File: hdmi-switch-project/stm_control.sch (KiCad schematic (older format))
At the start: 36 parts, among them U2 TCAN330, U3 STM32F103C8Tx

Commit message: Cosmetical changes, and VSDJ pin fixup
Signed-off-by: Andrej Manduch <amanduch@gmail.com>
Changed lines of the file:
@@
 encoding utf-8
 Sheet 4 4
-Title ""
-Date ""
+Title "HDMI Switch 4:2 modul"
+Date "2020-06-30"
 Rev ""
 Comp ""
-Comment1 ""
+Comment1 "Devel board"
 Comment2 ""
 Comment3 ""
@@
 $EndComp
 Entry Wire Line
-	4950 2450 5050 2550
-Entry Wire Line
-	4950 2550 5050 2650
-Entry Wire Line
-	4950 2750 5050 2850
-Entry Wire Line
-	4950 2850 5050 2950
-Entry Wire Line
-	4950 2950 5050 3050
-Entry Wire Line
-	4950 3950 5050 4050
-Entry Wire Line
-	4950 4050 5050 4150
-Entry Wire Line
-	4950 4150 5050 4250
-Entry Wire Line
-	4950 4250 5050 4350
-Wire Wire Line
-	5800 4350 5050 4350
-Wire Wire Line
-	5050 4250 5800 4250
-Wire Wire Line
-	5050 3050 5800 3050
-Wire Wire Line
-	5800 2950 5050 2950
-Wire Wire Line
-	5050 2850 5800 2850
-Wire Wire Line
-	5800 2650 5050 2650
-Wire Wire Line
-	5050 2550 5800 2550
+	5050 2450 5150 2550
+Entry Wire Line
+	5050 2550 5150 2650
+Entry Wire Line
+	5050 2750 5150 2850
+Entry Wire Line
+	5050 2850 5150 2950
+Entry Wire Line
+	5050 2950 5150 3050
+Entry Wire Line
+	5050 3950 5150 4050
+Entry Wire Line
+	5050 4050 5150 4150
+Entry Wire Line
+	5050 4150 5150 4250
+Entry Wire Line
+	5050 4250 5150 4350
+Wire Wire Line
+	5800 4350 5150 4350
+Wire Wire Line
+	5150 4250 5800 4250
+Wire Wire Line
+	5150 3050 5800 3050
+Wire Wire Line
+	5800 2950 5150 2950
+Wire Wire Line
+	5150 2850 5800 2850
+Wire Wire Line
+	5800 2650 5150 2650
+Wire Wire Line
+	5150 2550 5800 2550
 $Comp
 L Device:C C_XTAL11
@@
 Wire Wire Line
 	8850 2350 8950 2350
-Text Label 5050 2950 0    50   ~ 0
+Text Label 5150 2950 0    50   ~ 0
 XTAL2_RTC_A
-Text Label 5050 3050 0    50   ~ 0
+Text Label 5150 3050 0    50   ~ 0
 XTAL2_RTC_B
 Entry Wire Line
@@
 Text Label 10250 2800 0    50   ~ 0
 XTAL2_RTC_B
-Text Label 5050 2550 0    50   ~ 0
+Text Label 5150 2550 0    50   ~ 0
 XTAL1_A
-Text Label 5050 2650 0    50   ~ 0
+Text Label 5150 2650 0    50   ~ 0
 XTAL1_B
 $Comp
@@
 	1050 3150 1050 3100
 Entry Wire Line
-	7850 4650 7950 4750
-Entry Wire Line
-	7850 4550 7950 4650
-Entry Wire Line
-	7850 4450 7950 4550
-Entry Wire Line
-	7850 4350 7950 4450
-Wire Wire Line
-	7850 4350 7100 4350
-Wire Wire Line
-	7100 4450 7850 4450
+	7650 4650 7750 4750
+Entry Wire Line
+	7650 4550 7750 4650
+Entry Wire Line
+	7650 4450 7750 4550
+Entry Wire Line
+	7650 4350 7750 4450
+Wire Wire Line
+	7650 4350 7100 4350
+Wire Wire Line
+	7100 4450 7650 4450
 Text Label 7150 4350 0    50   ~ 0
 USB1_D-
@@
 $EndComp
 Wire Wire Line
-	7100 4650 7850 4650
+	7100 4650 7650 4650
 Text Label 7150 4650 0    50   ~ 0
 STM_SWDCLCK
 Wire Wire Line
-	7100 4550 7850 4550
+	7100 4550 7650 4550
 Text Label 7150 4550 0    50   ~ 0
 STM_SWDIO
@@
 Wire Notes Line
 	550  3300 550  5250
-Text Label 5050 3450 0    50   ~ 0
+Text Label 5150 3450 0    50   ~ 0
 STM_BOOT1
 Entry Wire Line
-	4950 2250 5050 2350
-Wire Wire Line
-	5800 2350 5050 2350
-Text Label 5050 2350 0    50   ~ 0
+	5050 2250 5150 2350
+Wire Wire Line
+	5800 2350 5150 2350
+Text Label 5150 2350 0    50   ~ 0
 STM_BOOT0
 $Comp
@@
 Wire Wire Line
 	2000 4950 2100 4950
-Text HLabel 5500 3850 0    50   Input ~ 0
+Text HLabel 5600 3850 0    50   Input ~ 0
 ST_H_CLK
-Text HLabel 5500 3950 0    50   Input ~ 0
+Text HLabel 5600 3950 0    50   Input ~ 0
 ST_H_SDA
 Wire Wire Line
-	5500 3850 5800 3850
-Wire Wire Line
-	5800 3950 5500 3950
-Wire Wire Line
-	5050 4050 5800 4050
-Wire Wire Line
-	5800 4150 5050 4150
-Text Label 5050 4050 0    50   ~ 0
+	5600 3850 5800 3850
+Wire Wire Line
+	5800 3950 5600 3950
+Wire Wire Line
+	5150 4050 5800 4050
+Wire Wire Line
+	5800 4150 5150 4150
+Text Label 5150 4050 0    50   ~ 0
 STM_CAN_RX
-Text Label 5050 4150 0    50   ~ 0
+Text Label 5150 4150 0    50   ~ 0
 STM_CAN_TX
-Text Label 5050 4350 0    50   ~ 0
+Text Label 5150 4350 0    50   ~ 0
 STM_CNTRL_SDA
-Text Label 5050 4250 0    50   ~ 0
+Text Label 5150 4250 0    50   ~ 0
 STM_CNTRL_CLK
 Text Label 7150 4250 0    50   ~ 0
@@
 STM_TX
 Entry Wire Line
-	7850 4250 7950 4350
-Entry Wire Line
-	7850 4150 7950 4250
-Wire Wire Line
-	7100 4150 7850 4150
-Wire Wire Line
-	7100 4250 7850 4250
+	7650 4250 7750 4350
+Entry Wire Line
+	7650 4150 7750 4250
+Wire Wire Line
+	7100 4150 7650 4150
+Wire Wire Line
+	7100 4250 7650 4250
 Text HLabel 7200 3250 2    50   Input ~ 0
 STM_GPIO0
@@
 STM_GPIO7
 Wire Wire Line
-	5050 3450 5800 3450
-Entry Wire Line
-	4950 3350 5050 3450
+	5150 3450 5800 3450
+Entry Wire Line
+	5050 3350 5150 3450
 Wire Wire Line
 	7200 3950 7100 3950
@@
 Wire Wire Line
 	7100 3250 7200 3250
-Text HLabel 5700 3350 0    50   Input ~ 0
+Text HLabel 5600 3350 0    50   Input ~ 0
 STM_GPIO
-Text HLabel 5700 3250 0    50   Input ~ 0
+Text HLabel 5600 3250 0    50   Input ~ 0
 STM_GE
-Text HLabel 5700 3550 0    50   Input ~ 0
+Text HLabel 5600 3550 0    50   Input ~ 0
 STM_A0
-Text HLabel 5700 3650 0    50   Input ~ 0
+Text HLabel 5600 3650 0    50   Input ~ 0
 STM_A1
 Wire Wire Line
-	5700 3250 5800 3250
-Wire Wire Line
-	5800 3350 5700 3350
-Wire Wire Line
-	5700 3550 5800 3550
-Wire Wire Line
-	5800 3650 5700 3650
+	5600 3250 5800 3250
+Wire Wire Line
+	5800 3350 5600 3350
+Wire Wire Line
+	5600 3550 5800 3550
+Wire Wire Line
+	5800 3650 5600 3650
 Text HLabel 7200 4050 2    50   Input ~ 0
 STM_GPIO8
@@
 Wire Wire Line
 	3200 1300 3200 1200
-Text Label 5050 2850 0    50   ~ 0
+Text Label 5150 2850 0    50   ~ 0
 STM_LED1
 $Comp
@@
 	5650 2150 5800 2150
 Entry Wire Line
-	4950 4650 5050 4750
-Wire Wire Line
-	5800 4750 5050 4750
-Text Label 5050 4750 0    50   ~ 0
+	5050 4650 5150 4750
+Wire Wire Line
+	5800 4750 5150 4750
+Text Label 5150 4750 0    50   ~ 0
 STM_BTN1
 Wire Notes Line
@@
 Wire Notes Line
 	4600 700  4600 3000
-Text HLabel 5700 3750 0    50   Input ~ 0
+Text HLabel 5600 3750 0    50   Input ~ 0
 STM_OVS
 Wire Wire Line
-	5800 3750 5700 3750
+	5800 3750 5600 3750
 Wire Bus Line
 	4200 2050 4200 2450
@@
 	10850 1450 10850 2950
 Wire Bus Line
-	7950 1900 7950 4850
+	7750 4150 7750 4850
 Wire Bus Line
-	4950 1850 4950 4850
+	5050 2200 5050 4850
 $EndSCHEMATC

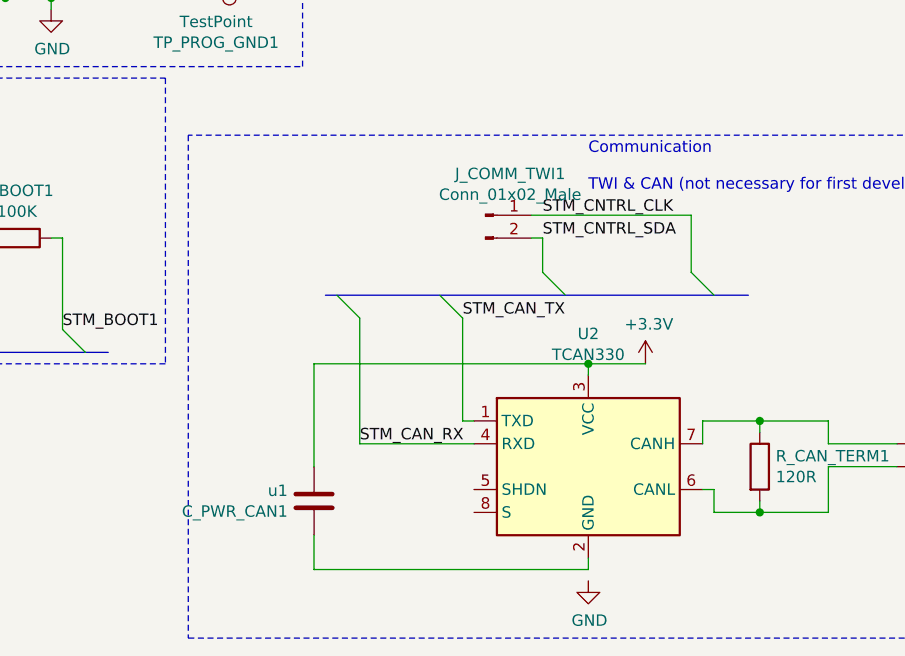
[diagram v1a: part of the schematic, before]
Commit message: Precission resistor changed
from 4k6 to 4k64 %1

Signed-off-by: Andrej Manduch <amanduch@gmail.com>
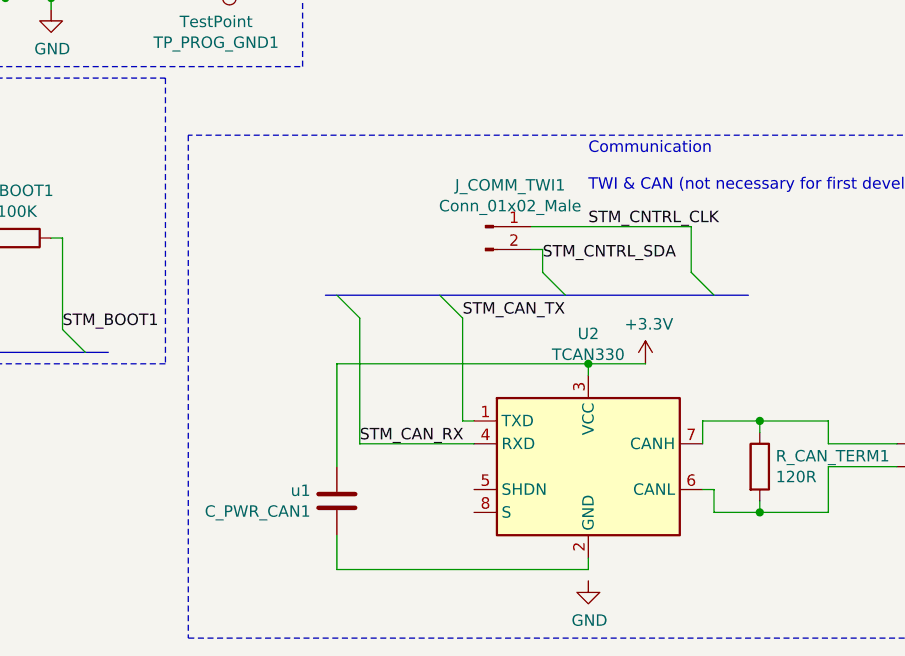
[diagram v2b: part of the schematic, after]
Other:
- moved on the sheet: C_PWR_CAN1, J_COMM_TWI1
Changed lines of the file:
@@
 	3650 6350 3650 6900
 Wire Wire Line
-	3450 6550 3450 7000
+	3550 6550 3550 7000
 Connection ~ 4650 6550
 Wire Wire Line
@@
 	4650 7450 4650 7400
 Wire Wire Line
-	3450 7450 4650 7450
-Wire Wire Line
-	3450 7300 3450 7450
-Wire Wire Line
-	4650 6550 3450 6550
+	3550 7450 4650 7450
+Wire Wire Line
+	3550 7300 3550 7450
+Wire Wire Line
+	4650 6550 3550 6550
 Wire Wire Line
 	4650 6600 4650 6550
-$Comp
-L Device:C C_PWR_CAN1
-U 1 1 5FF842AA
-P 3450 7150
-F 0 "C_PWR_CAN1" H 3565 7196 50  0000 L CNN
-F 1 "u1" H 3565 7105 50  0000 L CNN
-F 2 "" H 3488 7000 50  0001 C CNN
-F 3 "~" H 3450 7150 50  0001 C CNN
-	1    3450 7150
-	-1   0    0    1
-$EndComp
 Wire Wire Line
 	3650 6900 4150 6900
@@
 $EndComp
 Wire Wire Line
-	4400 5900 5100 5900
-Text Label 4450 5900 0    50   ~ 0
+	4400 5950 5100 5950
+Text Label 4650 5950 0    50   ~ 0
 STM_CNTRL_CLK
-Text Label 4450 6000 0    50   ~ 0
+Text Label 4450 6100 0    50   ~ 0
 STM_CNTRL_SDA
 Wire Wire Line
-	5100 6150 5100 5900
-Wire Wire Line
-	4450 6000 4400 6000
+	5100 6150 5100 5950
+Wire Wire Line
+	4450 6050 4400 6050
 Entry Wire Line
 	5100 6150 5200 6250
@@
 	4450 6150 4550 6250
 Wire Wire Line
-	4450 6150 4450 6000
+	4450 6150 4450 6050
 $Comp
 L Connector:Conn_01x02_Male J_COMM_TWI1
 U 1 1 5FE65265
-P 4200 5900
-F 0 "J_COMM_TWI1" H 4308 6081 50  0000 C CNN
-F 1 "Conn_01x02_Male" H 4308 5990 50  0000 C CNN
-F 2 "" H 4200 5900 50  0001 C CNN
-F 3 "~" H 4200 5900 50  0001 C CNN
-	1    4200 5900
+P 4200 5950
+F 0 "J_COMM_TWI1" H 4308 6131 50  0000 C CNN
+F 1 "Conn_01x02_Male" H 4308 6040 50  0000 C CNN
+F 2 "" H 4200 5950 50  0001 C CNN
+F 3 "~" H 4200 5950 50  0001 C CNN
+	1    4200 5950
 	1    0    0    -1
 $EndComp
@@
 Wire Wire Line
 	5800 3750 5600 3750
+$Comp
+L Device:C C_PWR_CAN1
+U 1 1 5FF842AA
+P 3550 7150
+F 0 "C_PWR_CAN1" H 3665 7196 50  0000 L CNN
+F 1 "u1" H 3665 7105 50  0000 L CNN
+F 2 "" H 3588 7000 50  0001 C CNN
+F 3 "~" H 3550 7150 50  0001 C CNN
+	1    3550 7150
+	-1   0    0    1
+$EndComp
 Wire Bus Line
 	4200 2050 4200 2450

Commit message: placed UART connector
Signed-off-by: Andrej Manduch <amanduch@gmail.com>
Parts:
- added J_UART: Conn_01x03_Male, symbol Connector:Conn_01x03_Male
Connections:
- net GND: now also J_UART.3 (Pin_3)
- net STM_RX: now also J_UART.2 (Pin_2)
- net STM_TX: now also J_UART.1 (Pin_1)
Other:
- note added: "Service UART"
- moved on the sheet: C_BUTTON1, D_LED1, R_BTN1, R_LED1, SW_STM1
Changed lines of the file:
@@
 L power:+3.3V #PWR020
 U 1 1 6001D411
-P 3200 1200
-F 0 "#PWR020" H 3200 1050 50  0001 C CNN
-F 1 "+3.3V" H 3215 1373 50  0000 C CNN
-F 2 "" H 3200 1200 50  0001 C CNN
-F 3 "" H 3200 1200 50  0001 C CNN
-	1    3200 1200
-	1    0    0    -1
-$EndComp
-Wire Wire Line
-	3200 1300 3200 1200
+P 3050 1050
+F 0 "#PWR020" H 3050 900 50  0001 C CNN
+F 1 "+3.3V" H 3065 1223 50  0000 C CNN
+F 2 "" H 3050 1050 50  0001 C CNN
+F 3 "" H 3050 1050 50  0001 C CNN
+	1    3050 1050
+	1    0    0    -1
+$EndComp
+Wire Wire Line
+	3050 1150 3050 1050
 Text Label 5150 2850 0    50   ~ 0
 STM_LED1
@@
 STM_BTN1
 Wire Notes Line
-	4400 1550 4400 3000
-Text Notes 3750 1800 0    50   ~ 0
+	4250 1400 4250 2850
+Text Notes 3600 1650 0    50   ~ 0
 Example Button
 Entry Wire Line
-	4100 2200 4200 2300
-Wire Wire Line
-	3600 2200 4100 2200
-Text Label 3700 2200 0    50   ~ 0
+	3950 2050 4050 2150
+Wire Wire Line
+	3450 2050 3950 2050
+Text Label 3550 2050 0    50   ~ 0
 STM_BTN1
-Connection ~ 3600 2700
-Wire Wire Line
-	3600 2750 3600 2700
-Wire Wire Line
-	3600 1850 3600 1800
-Connection ~ 3600 2200
-Wire Wire Line
-	3600 2200 3600 2150
+Connection ~ 3450 2550
+Wire Wire Line
+	3450 2600 3450 2550
+Wire Wire Line
+	3450 1700 3450 1650
+Connection ~ 3450 2050
+Wire Wire Line
+	3450 2050 3450 2000
 $Comp
 L power:+3.3V #PWR021
 U 1 1 600B8EEF
-P 3600 1800
-F 0 "#PWR021" H 3600 1650 50  0001 C CNN
-F 1 "+3.3V" H 3615 1973 50  0000 C CNN
-F 2 "" H 3600 1800 50  0001 C CNN
-F 3 "" H 3600 1800 50  0001 C CNN
-	1    3600 1800
+P 3450 1650
+F 0 "#PWR021" H 3450 1500 50  0001 C CNN
+F 1 "+3.3V" H 3465 1823 50  0000 C CNN
+F 2 "" H 3450 1650 50  0001 C CNN
+F 3 "" H 3450 1650 50  0001 C CNN
+	1    3450 1650
 	1    0    0    -1
 $EndComp
@@
 L Device:R R_BTN1
 U 1 1 600B8B61
-P 3600 2000
-F 0 "R_BTN1" H 3670 2046 50  0000 L CNN
-F 1 "10K" H 3670 1955 50  0000 L CNN
-F 2 "" V 3530 2000 50  0001 C CNN
-F 3 "~" H 3600 2000 50  0001 C CNN
-	1    3600 2000
+P 3450 1850
+F 0 "R_BTN1" H 3520 1896 50  0000 L CNN
+F 1 "10K" H 3520 1805 50  0000 L CNN
+F 2 "" V 3380 1850 50  0001 C CNN
+F 3 "~" H 3450 1850 50  0001 C CNN
+	1    3450 1850
 	1    0    0    -1
 $EndComp
@@
 L power:GND #PWR022
 U 1 1 600B8434
-P 3600 2750
-F 0 "#PWR022" H 3600 2500 50  0001 C CNN
-F 1 "GND" H 3605 2577 50  0000 C CNN
-F 2 "" H 3600 2750 50  0001 C CNN
-F 3 "" H 3600 2750 50  0001 C CNN
-	1    3600 2750
-	1    0    0    -1
-$EndComp
-Wire Wire Line
-	3600 2700 3600 2600
-Wire Wire Line
-	3450 2700 3600 2700
-Wire Wire Line
-	3450 2650 3450 2700
-Wire Wire Line
-	3600 2200 3600 2300
-Wire Wire Line
-	3450 2200 3600 2200
-Wire Wire Line
-	3450 2250 3450 2200
+P 3450 2600
+F 0 "#PWR022" H 3450 2350 50  0001 C CNN
+F 1 "GND" H 3455 2427 50  0000 C CNN
+F 2 "" H 3450 2600 50  0001 C CNN
+F 3 "" H 3450 2600 50  0001 C CNN
+	1    3450 2600
+	1    0    0    -1
+$EndComp
+Wire Wire Line
+	3450 2550 3450 2450
+Wire Wire Line
+	3300 2550 3450 2550
+Wire Wire Line
+	3300 2500 3300 2550
+Wire Wire Line
+	3450 2050 3450 2150
+Wire Wire Line
+	3300 2050 3450 2050
+Wire Wire Line
+	3300 2100 3300 2050
 $Comp
 L Device:C C_BUTTON1
 U 1 1 60092EA5
-P 3600 2450
-F 0 "C_BUTTON1" H 3715 2496 50  0000 L CNN
-F 1 "u1" H 3715 2405 50  0000 L CNN
-F 2 "" H 3638 2300 50  0001 C CNN
-F 3 "~" H 3600 2450 50  0001 C CNN
-	1    3600 2450
+P 3450 2300
+F 0 "C_BUTTON1" H 3565 2346 50  0000 L CNN
+F 1 "u1" H 3565 2255 50  0000 L CNN
+F 2 "" H 3488 2150 50  0001 C CNN
+F 3 "~" H 3450 2300 50  0001 C CNN
+	1    3450 2300
 	1    0    0    -1
 $EndComp
@@
 L Switch:SW_Push SW_STM1
 U 1 1 600923F3
-P 3450 2450
-F 0 "SW_STM1" H 3450 2735 50  0000 C CNN
-F 1 "SW_Push" H 3450 2644 50  0000 C CNN
-F 2 "" H 3450 2650 50  0001 C CNN
-F 3 "~" H 3450 2650 50  0001 C CNN
-	1    3450 2450
+P 3300 2300
+F 0 "SW_STM1" H 3300 2585 50  0000 C CNN
+F 1 "SW_Push" H 3300 2494 50  0000 C CNN
+F 2 "" H 3300 2500 50  0001 C CNN
+F 3 "~" H 3300 2500 50  0001 C CNN
+	1    3300 2300
 	0    -1   -1   0
 $EndComp
 Wire Notes Line
-	4600 850  3100 850
-Text Notes 3650 950  0    50   ~ 0
+	4450 700  2950 700
+Text Notes 3500 800  0    50   ~ 0
 Example LED
 Entry Wire Line
-	4450 1300 4550 1400
-Wire Wire Line
-	4450 1300 4150 1300
-Text Label 4150 1300 0    50   ~ 0
+	4300 1150 4400 1250
+Wire Wire Line
+	4300 1150 4000 1150
+Text Label 4000 1150 0    50   ~ 0
 STM_LED1
 Wire Wire Line
-	3350 1300 3200 1300
-Wire Wire Line
-	3850 1300 3650 1300
+	3200 1150 3050 1150
+Wire Wire Line
+	3700 1150 3500 1150
 $Comp
 L Device:R R_LED1
 U 1 1 6001490B
-P 4000 1300
-F 0 "R_LED1" V 3793 1300 50  0000 C CNN
-F 1 "510R" V 3884 1300 50  0000 C CNN
-F 2 "" V 3930 1300 50  0001 C CNN
-F 3 "~" H 4000 1300 50  0001 C CNN
-	1    4000 1300
+P 3850 1150
+F 0 "R_LED1" V 3643 1150 50  0000 C CNN
+F 1 "510R" V 3734 1150 50  0000 C CNN
+F 2 "" V 3780 1150 50  0001 C CNN
+F 3 "~" H 3850 1150 50  0001 C CNN
+	1    3850 1150
 	0    1    1    0
 $EndComp
@@
 L Device:LED D_LED1
 U 1 1 60013E2E
-P 3500 1300
-F 0 "D_LED1" H 3493 1045 50  0000 C CNN
-F 1 "LED" H 3493 1136 50  0000 C CNN
-F 2 "" H 3500 1300 50  0001 C CNN
-F 3 "~" H 3500 1300 50  0001 C CNN
-	1    3500 1300
+P 3350 1150
+F 0 "D_LED1" H 3343 895 50  0000 C CNN
+F 1 "LED" H 3343 986 50  0000 C CNN
+F 2 "" H 3350 1150 50  0001 C CNN
+F 3 "~" H 3350 1150 50  0001 C CNN
+	1    3350 1150
 	-1   0    0    1
 $EndComp
@@
 	3400 3300 550  3300
 Wire Notes Line
-	3100 1550 4600 1550
-Text Notes 3150 800  0    50   ~ 0
+	2950 1400 4450 1400
+Text Notes 3000 650  0    50   ~ 0
 Devel board only
 Wire Notes Line
-	3100 700  4600 700
-Wire Notes Line
-	3100 700  3100 3000
-Wire Notes Line
-	3100 3000 4600 3000
-Wire Notes Line
-	4600 700  4600 3000
+	2950 550  4450 550
+Wire Notes Line
+	2950 550  2950 2850
+Wire Notes Line
+	2950 2850 4450 2850
+Wire Notes Line
+	4450 550  4450 2850
 Text HLabel 5600 3750 0    50   Input ~ 0
 STM_OVS
@@
 	-1   0    0    1
 $EndComp
-Wire Bus Line
-	4200 2050 4200 2450
-Wire Bus Line
-	4550 1200 4550 1500
+$Comp
+L Connector:Conn_01x03_Male J_UART
+U 1 1 5F05E7E6
+P 10100 3850
+F 0 "J_UART" H 10208 4131 50  0000 C CNN
+F 1 "Conn_01x03_Male" H 10208 4040 50  0000 C CNN
+F 2 "" H 10100 3850 50  0001 C CNN
+F 3 "~" H 10100 3850 50  0001 C CNN
+	1    10100 3850
+	1    0    0    -1
+$EndComp
+Entry Wire Line
+	10750 3750 10850 3850
+Entry Wire Line
+	10750 3850 10850 3950
+Wire Wire Line
+	10750 3750 10300 3750
+Wire Wire Line
+	10300 3850 10750 3850
+Text Label 10350 3750 0    50   ~ 0
+STM_TX
+Text Label 10350 3850 0    50   ~ 0
+STM_RX
+$Comp
+L power:GND #PWR?
+U 1 1 5F0997C1
+P 10400 4050
+F 0 "#PWR?" H 10400 3800 50  0001 C CNN
+F 1 "GND" H 10405 3877 50  0000 C CNN
+F 2 "" H 10400 4050 50  0001 C CNN
+F 3 "" H 10400 4050 50  0001 C CNN
+	1    10400 4050
+	1    0    0    -1
+$EndComp
+Wire Wire Line
+	10300 3950 10400 3950
+Wire Wire Line
+	10400 3950 10400 4050
+Text Notes 10250 3450 0    50   ~ 0
+Service UART
+Wire Notes Line
+	10900 4300 10900 3350
+Wire Notes Line
+	10900 3350 9850 3350
+Wire Notes Line
+	9850 3350 9850 4300
+Wire Notes Line
+	9850 4300 10900 4300
+Wire Bus Line
+	4050 1900 4050 2300
+Wire Bus Line
+	4400 1050 4400 1350
 Wire Bus Line
 	2750 2400 2750 3050
@@
 	650  6500 2550 6500
 Wire Bus Line
+	10850 3700 10850 4050
+Wire Bus Line
 	3500 6250 5350 6250
